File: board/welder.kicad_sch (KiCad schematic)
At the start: 71 parts, among them J1 VIN, J2 Conn_01x10, J3 Barrel_Jack_Switch, J4 USB_B, J5 POS, J6 NEG, J7 GND, J8 EXT, Q1 Q_NIGBT_GCE, Q2 Q_NIGBT_GCE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

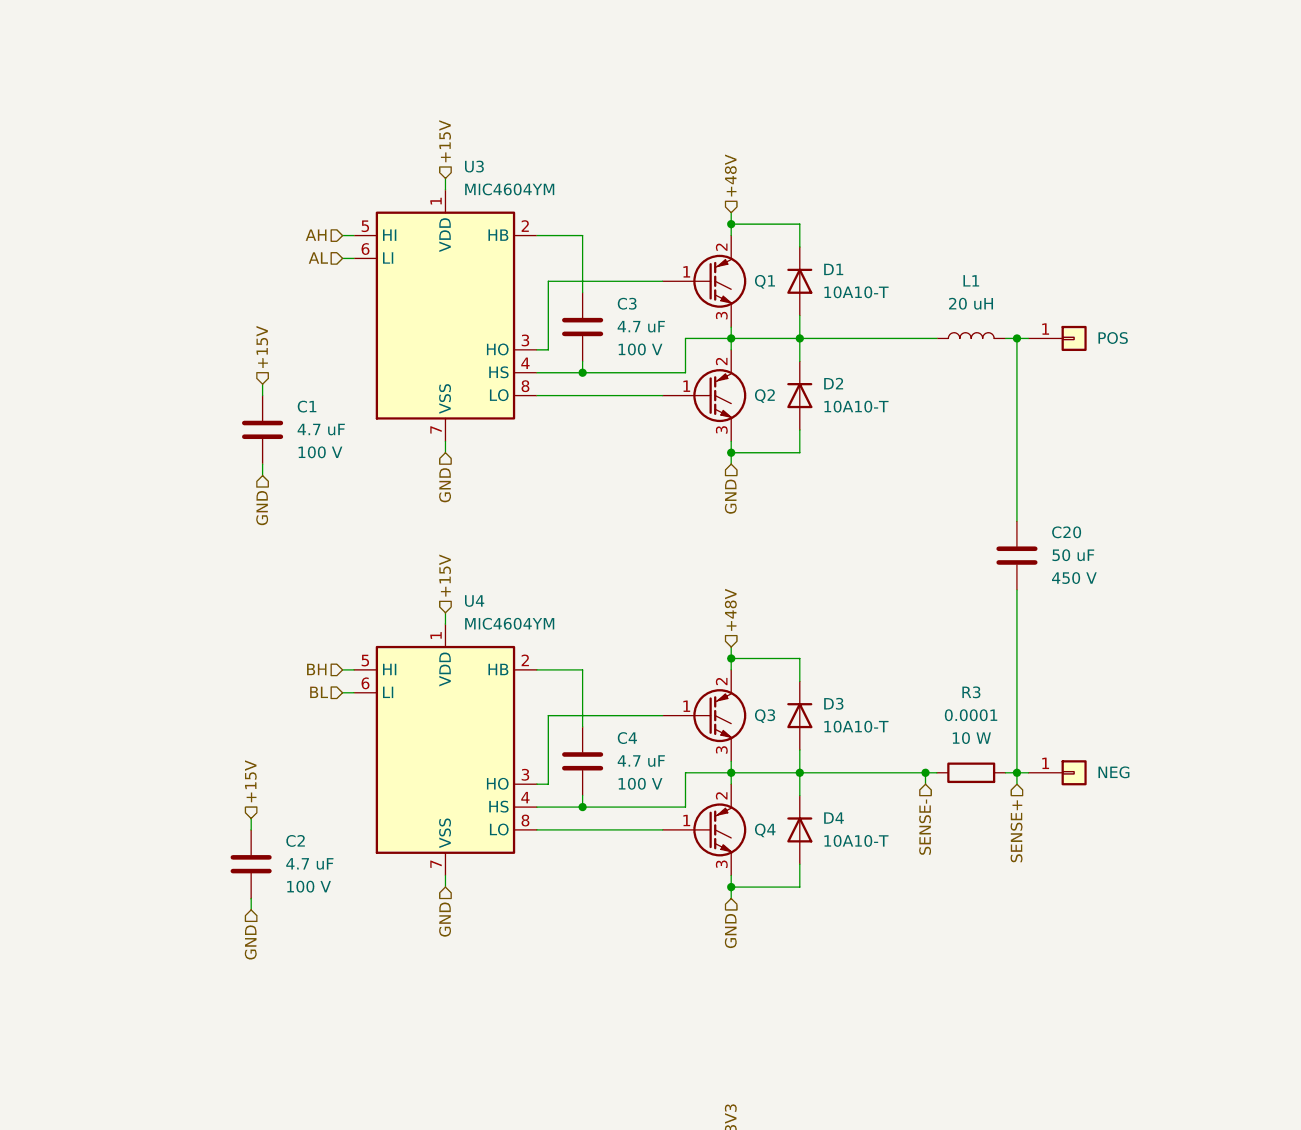
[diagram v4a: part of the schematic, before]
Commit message: Added Rg and HS protection
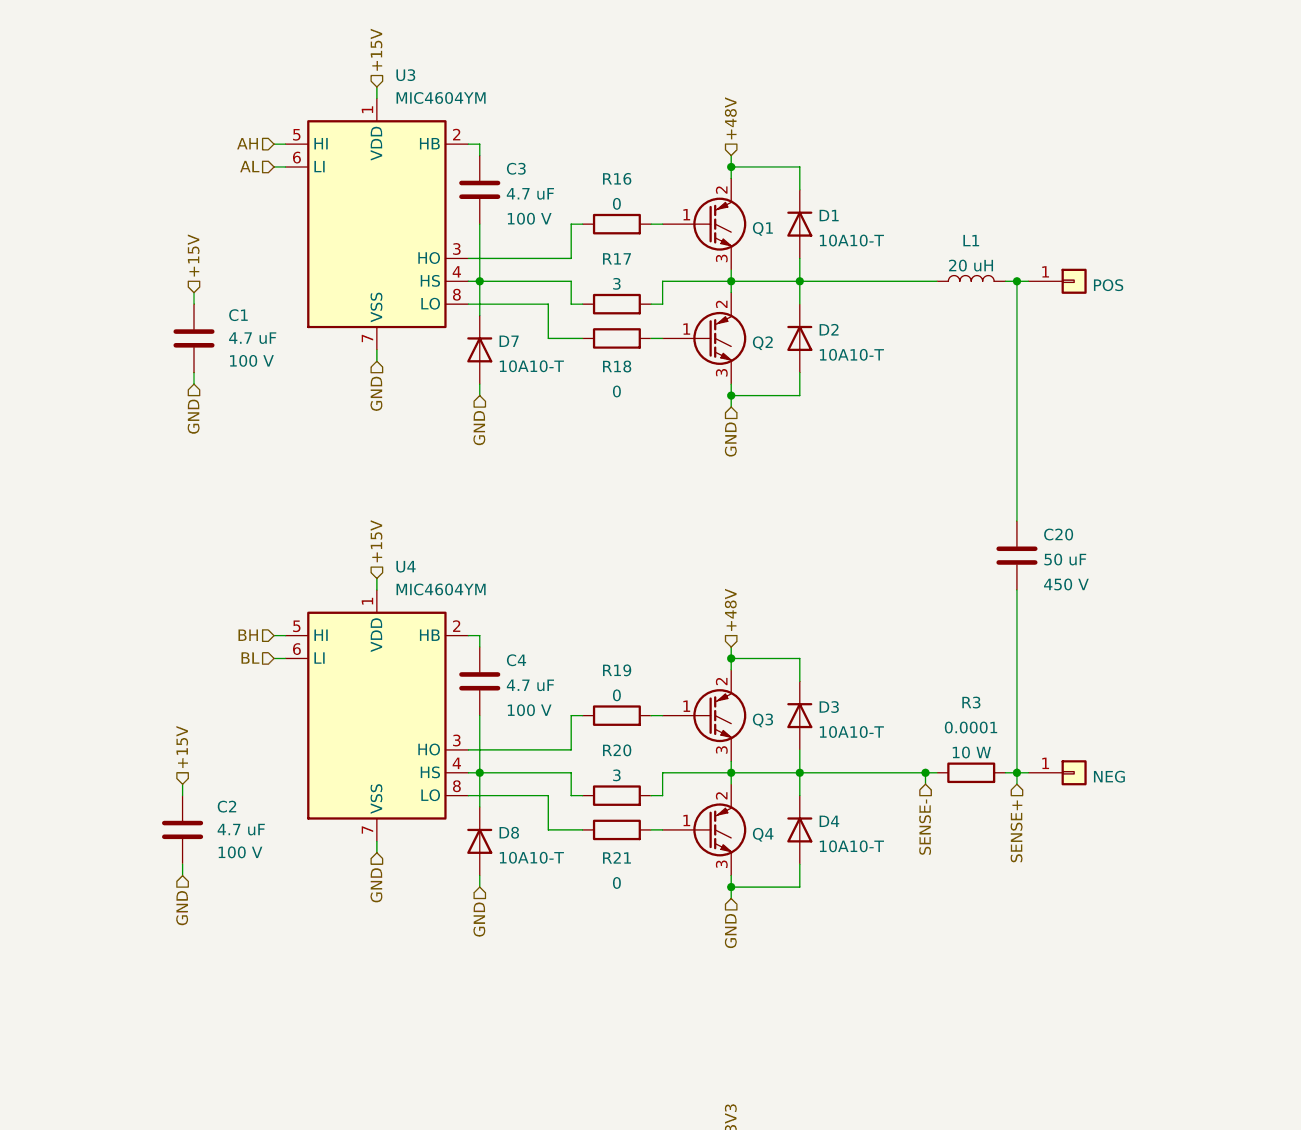
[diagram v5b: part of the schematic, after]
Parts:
- added D7, D8: 10A10-T, Diode_THT:D_P600_R-6_P7.62mm_Vertical_AnodeUp, symbol Device:D
- added R16, R18, R19, R21: 0, Resistor_SMD:R_0805_2012Metric, symbol Device:R
- added R17, R20: 3, Resistor_SMD:R_0805_2012Metric, symbol Device:R
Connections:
- net GND: now also D7.2 (A), D8.2 (A)
- net SENSE-: now also R20.2; no longer C4.1, U4.4 (HS)
- net at U4.3 (HO): now also R19.1; no longer Q3.1 (G)
- net at U4.8 (LO): now also R21.1; no longer Q4.1 (G)
- net at D1.2 (A), D2.1 (K), L1.1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: now also R17.2; no longer C3.1, U3.4 (HS)
- net at Q2.1 (G): now also R18.2; no longer U3.8 (LO)
- net at U3.3 (HO): now also R16.1; no longer Q1.1 (G)
- new net: Q4.1 (G), R21.2
- new net: C4.1, D8.1 (K), R20.1, U4.4 (HS)
- new net: Q3.1 (G), R19.2
- new net: C3.1, D7.1 (K), R17.1, U3.4 (HS)
- new net: R18.1, U3.8 (LO)
- new net: Q1.1 (G), R16.2
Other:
- moved on the sheet: C1, C2, C3, C4, D1, D2, L1, Q1, Q2, U3, U4

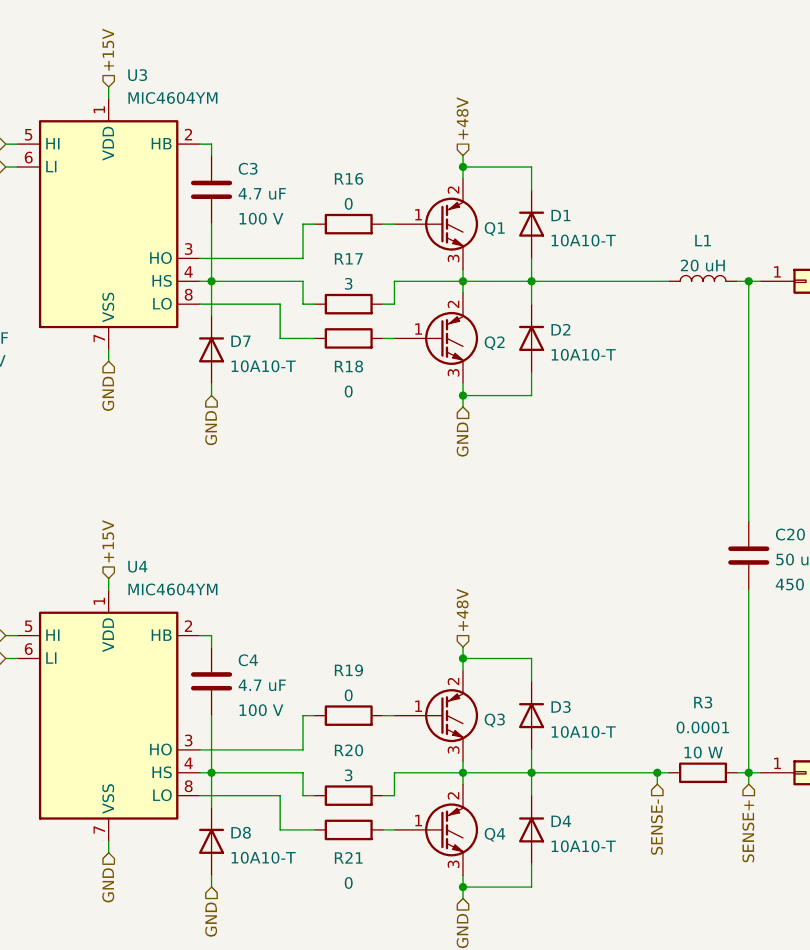
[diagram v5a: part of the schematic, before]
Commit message: add heatsinks
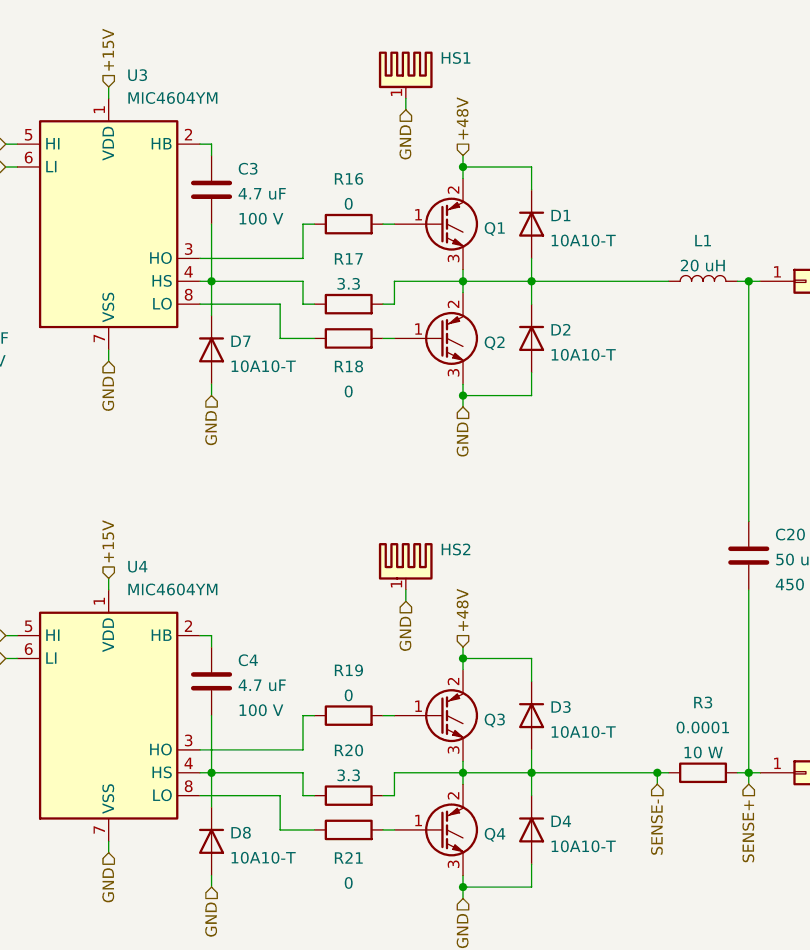
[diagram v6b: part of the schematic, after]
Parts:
- added HS1, HS2: Heatsink_Pad, colinholzman:Ohmite_C60-075, symbol Mechanical:Heatsink_Pad
- R10, R11, R4, R5, R6, R7, R8, R9: mfg1 (none) -> Xicon; mfg1pn (none) -> 260-220-RC
- R12, R13, R14, R15: mfg1 (none) -> Bourns; mfg1pn (none) -> CR0805-JW-471ELF
- R16, R18, R19, R21: mfg1 (none) -> YAGEO; mfg1pn (none) -> AC0805JR-070RL
- R17, R20: value 3 -> 3.3; footprint Resistor_SMD:R_0805_2012Metric -> Resistor_SMD:R_1206_3216Metric; Power (none) -> 0.66 W; description Resistor, 3 Ohm, 0805 -> Resistor, 3.3 Ohm, 0.66 W, 1206; mfg1 (none) -> Panasonic; mfg1pn (none) -> ERJ-P08J3R3V
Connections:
- net GND: now also HS1.1, HS2.1
